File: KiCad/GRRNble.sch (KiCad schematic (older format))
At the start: 47 parts, among them J1 JST_SH_06, Q1 DMG3415U, Q2 BSS138, Q3 DMG3415U, SW1 SW_Push, SW2 SW_Push, SW3 SW_Push, U1 R5F100LJAFB, U2 BUZZER, U3 SSD1306, U4 MCP73831, U5 RN4020, U6 MCP1703A-3302_SOT23, Y1 32.768k

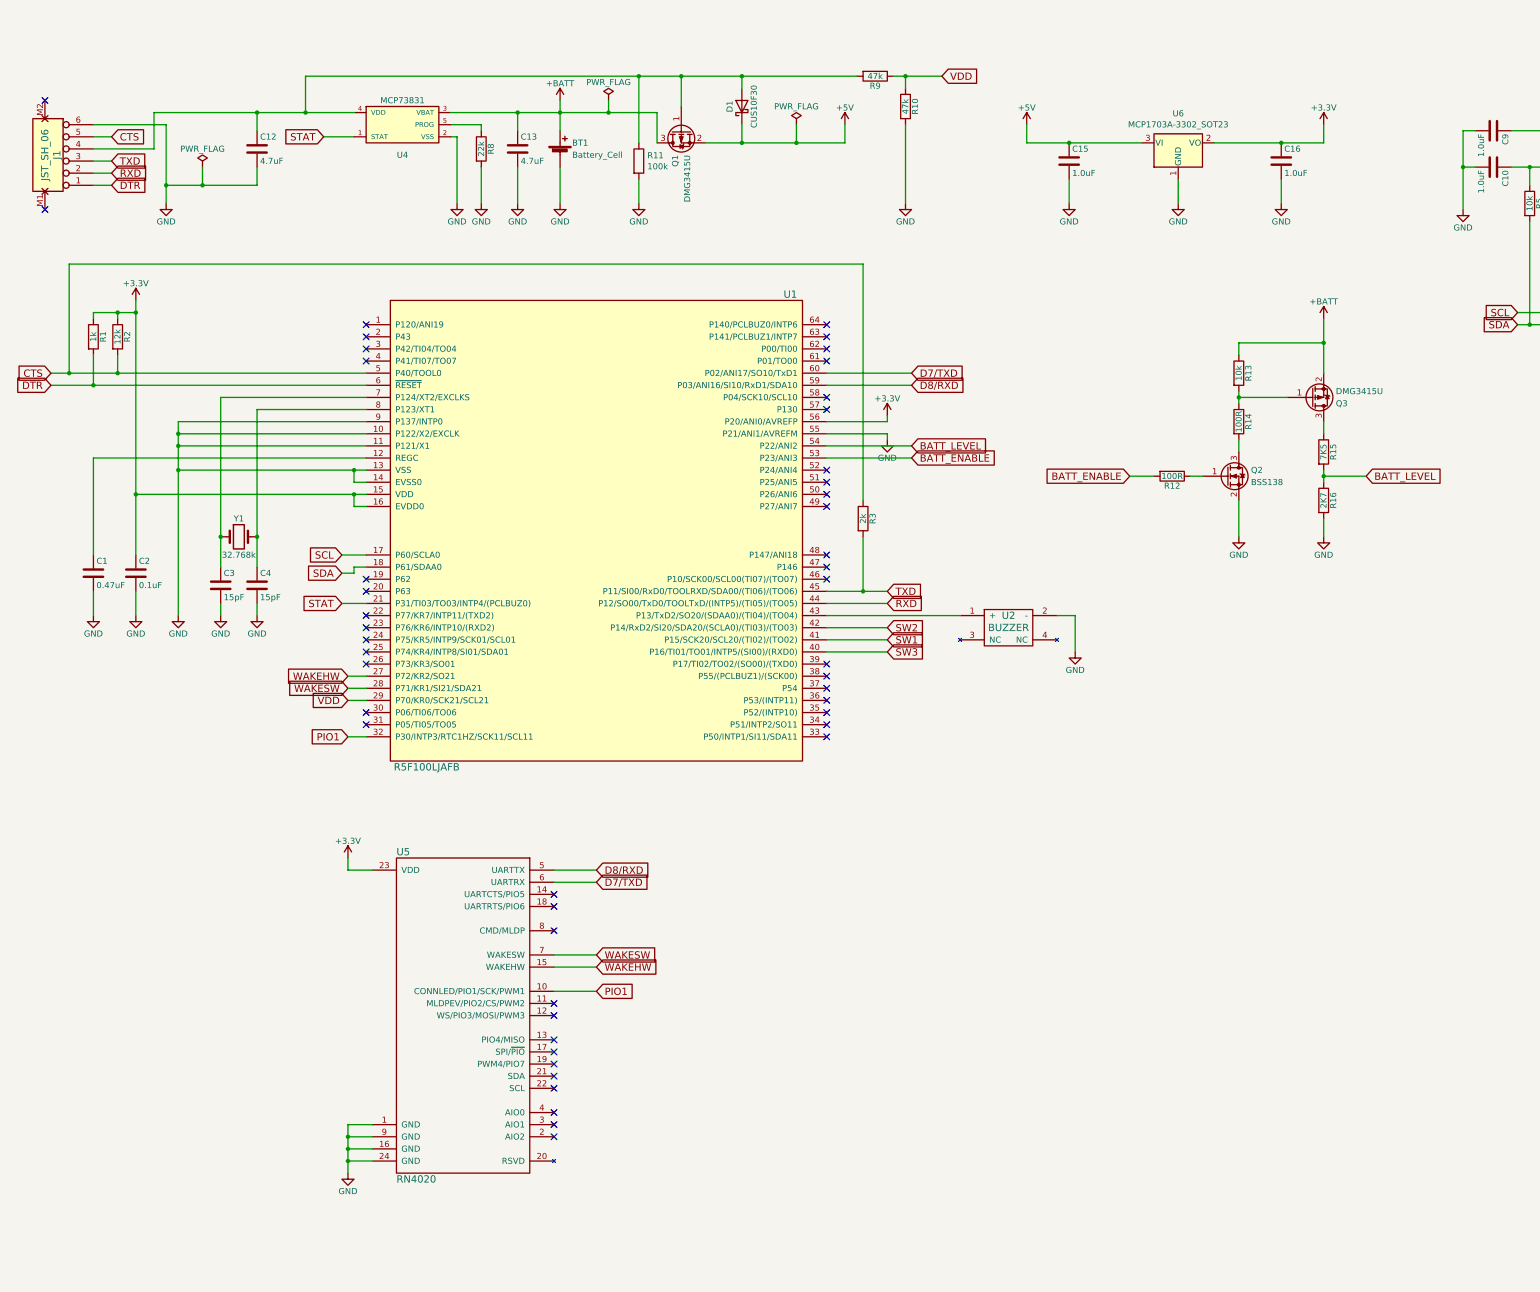
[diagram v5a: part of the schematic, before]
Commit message: change PCB layout
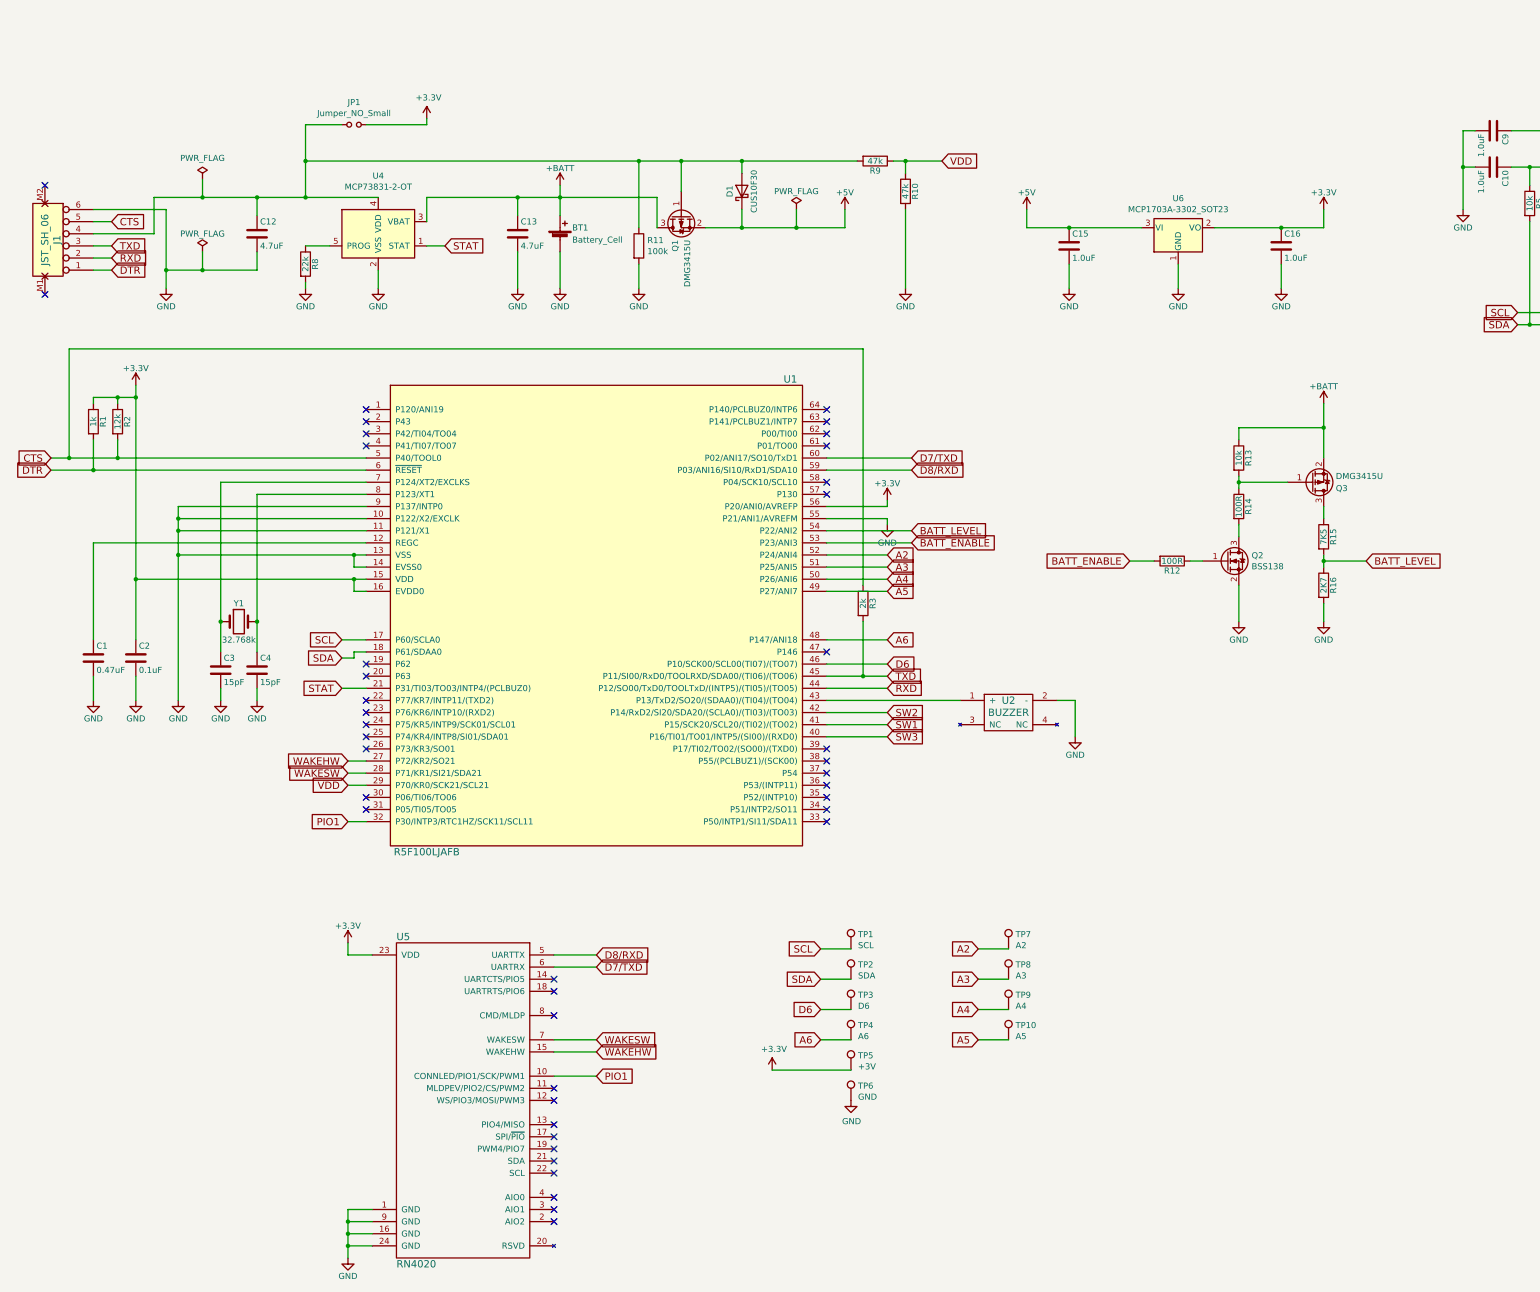
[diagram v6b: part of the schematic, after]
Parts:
- removed Q2: BSS138, TO_SOT_Packages_SMD:SOT-23, symbol GRRNble-rescue:Q_NMOS_GSD
- removed U4: MCP73831, TO_SOT_Packages_SMD:SOT-23-5_HandSoldering, symbol open-project:MCP73831
- added JP1: Jumper_NO_Small, Jumper:SolderJumper-2_P1.3mm_Open_RoundedPad1.0x1.5mm, symbol Device:Jumper_NO_Small
- added Q2: BSS138, Package_TO_SOT_SMD:SOT-23, symbol Transistor_FET:BSS138
- added TP1: SCL, TestPoint:TestPoint_THTPad_D1.0mm_Drill0.5mm, symbol Connector:TestPoint
- added TP10: A5, TestPoint:TestPoint_Pad_D1.0mm, symbol Connector:TestPoint
- added TP2: SDA, TestPoint:TestPoint_THTPad_D1.0mm_Drill0.5mm, symbol Connector:TestPoint
- added TP3: D6, TestPoint:TestPoint_THTPad_D1.0mm_Drill0.5mm, symbol Connector:TestPoint
- added TP4: A6, TestPoint:TestPoint_THTPad_D1.0mm_Drill0.5mm, symbol Connector:TestPoint
- added TP5: +3V, TestPoint:TestPoint_THTPad_D1.0mm_Drill0.5mm, symbol Connector:TestPoint
- added TP6: GND, TestPoint:TestPoint_THTPad_1.0x1.0mm_Drill0.5mm, symbol Connector:TestPoint
- added TP7: A2, TestPoint:TestPoint_Pad_D1.0mm, symbol Connector:TestPoint
- added TP8: A3, TestPoint:TestPoint_Pad_D1.0mm, symbol Connector:TestPoint
- added TP9: A4, TestPoint:TestPoint_Pad_D1.0mm, symbol Connector:TestPoint
- added U4: MCP73831-2-OT, Package_TO_SOT_SMD:SOT-23-5, symbol Battery_Management:MCP73831-2-OT
- C1, C10, C11, C12, C13, C15, C16, C2, C3, C4, C5, C6, C7, C8, C9: footprint Capacitors_SMD:C_0805_HandSoldering -> Capacitor_SMD:C_0805_2012Metric_Pad1.15x1.40mm_HandSolder
- D1: footprint Diodes_SMD:D_SOD-323_HandSoldering -> Diode_SMD:D_SOD-323_HandSoldering
- Q1, Q3: footprint TO_SOT_Packages_SMD:SOT-23 -> Package_TO_SOT_SMD:SOT-23
- R1, R10, R12, R13, R14, R15, R16, R2, R3, R4, R5, R6, R7, R8, R9: footprint Resistors_SMD:R_0805_HandSoldering -> Resistor_SMD:R_0805_2012Metric_Pad1.15x1.40mm_HandSolder
- U1: footprint Housings_QFP:LQFP-64_10x10mm_Pitch0.5mm -> Package_QFP:LQFP-64_10x10mm_P0.5mm
- Y1: footprint Crystals:Crystal_SMD_G8-2pin_3.2x1.5mm_HandSoldering -> Crystal:Crystal_SMD_G8-2Pin_3.2x1.5mm_HandSoldering
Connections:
- net +3V3: now also JP1.2, TP5.1
- net +BATT: now also U4.3 (VBAT)
- net GND: now also Q2.2 (S), TP6.1, U4.2 (VSS)
- net SCL: now also TP1.1
- net SDA: now also TP2.1
- net STAT: now also U4.1 (STAT)
- net D6: now reaches U1.46 (P10/SCK00/SCL00(TI07)/(TO07))
- net D6: now also TP3.1
- net A6: now reaches U1.48 (P147/ANI18)
- net A6: now also TP4.1
- net A5: now reaches U1.49 (P27/ANI7)
- net A5: now also TP10.1
- net A4: now reaches U1.50 (P26/ANI6)
- net A4: now also TP9.1
- net A3: now reaches U1.51 (P25/ANI5)
- net A3: now also TP8.1
- net A2: now reaches U1.52 (P24/ANI4)
- net A2: now also TP7.1
- net at C12.1, D1.2 (A), J1.4 (P4)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: now also JP1.1, U4.4 (VDD)
- net at R8.1: now also U4.5 (PROG)
- net at R14.2: now also Q2.3 (D)
- net at R12.1: now also Q2.1 (G)
- no-connect marks 48 -> 42
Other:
- moved on the sheet: BT1, C1, C12, C13, C15, C16, C2, C3, C4, D1, J1, Q1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
